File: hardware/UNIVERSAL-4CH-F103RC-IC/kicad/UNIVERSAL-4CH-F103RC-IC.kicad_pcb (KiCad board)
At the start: 2 copper layers, 124 x 93 mm, 145 parts, among them J1 ACTUATOR_CH1_4P, J2 ACTUATOR_CH2_4P, J201 REED_A_OPEN_5V_SIG_GND_PROTEC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, J202 REED_A_CLOSED_5V_SIG_GND_PROT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, J203 REED_A_IN_PLACE_5V_SIG_GND_PR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, J211 CAP_CS1_GND, J212 CAP_CS2_GND, J213 CAP_CS3_GND, J220 SWD_S1_3V3_DIO_CLK_NRST_GND, J230 LOGIC_12V_GND, J240 CANH_CANL_GND_SHIELD, J280B WIRE_FROM_C280_POS, J3 ACTUATOR_CH3_4P, J4 ACTUATOR_CH4_4P, U1 VNH5019A-E, U2 VNH5019A-E, U230 AMS1117-3V3, U250 25LC256_SOIC8_CARRIER_ID, U270 TLV6700DDCR_POWER_MONITOR, U3 VNH5019A-E, U300 STM32F103RCT6, U4 VNH5019A-E, Y300 8MHz

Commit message: Reinforce four-channel motor layer transitions
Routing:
- net CH4_OUTB: track 43.7 -> 48.5 mm, vias 1 -> 4
- net CH4_OUTA: vias 10 -> 22
- net CH3_OUTA: vias 8 -> 20
- net CH2_OUTA: vias 3 -> 5
- net CH1_OUTA: vias 3 -> 5

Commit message: Expand channel 1 and 2 power via banks
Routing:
- net CH2_OUTA: track 51.1 -> 52.7 mm, vias 5 -> 7
- net CH1_OUTA: vias 5 -> 10
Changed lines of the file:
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@@
+	)
+	(segment
+		(start 52.5 25.75)
+		(end 52.5 26.55)
+		(width 0.6)
+		(layer "F.Cu")
+		(net "CH2_OUTA")
 	)
 	(segment
@@
 	)
 	(via
+		(at 52.5 26.55)
+		(size 0.8)
+		(drill 0.4)
+		(layers "F.Cu" "B.Cu")
+		(net "CH2_OUTA")
+	)
+	(via
 		(at 53.8051 25.109)
 		(size 0.6)
 		(drill 0.3)
+		(layers "F.Cu" "B.Cu")
+		(net "CH2_OUTA")
+	)
+	(via
+		(at 52.5 25.75)
+		(size 0.8)
+		(drill 0.4)
 		(layers "F.Cu" "B.Cu")
 		(net "CH2_OUTA")
@@
 	)
 	(segment
+		(start 52.5 25.75)
+		(end 52.5 26.55)
+		(width 0.6)
+		(layer "B.Cu")
+		(net "CH2_OUTA")
+	)
+	(segment
 		(start 44.6993 17.5)
 		(end 46.6483 19.449)
@@
 	)
 	(via
+		(at 16 30.5)
+		(size 0.8)
+		(drill 0.4)
+		(layers "F.Cu" "B.Cu")
+		(net "CH1_OUTA")
+	)
+	(via
 		(at 14.9983 32.9423)
 		(size 0.6)
@@
 	)
 	(via
+		(at 14.5 30.5)
+		(size 0.8)
+		(drill 0.4)
+		(layers "F.Cu" "B.Cu")
+		(net "CH1_OUTA")
+	)
+	(via
 		(at 15.6483 32.9423)
 		(size 0.6)
@@
 	)
 	(via
+		(at 14.5 31.5)
+		(size 0.8)
+		(drill 0.4)
+		(layers "F.Cu" "B.Cu")
+		(net "CH1_OUTA")
+	)
+	(via
 		(at 7.3767 32.9423)
 		(size 0.6)
@@
 	)
 	(via
+		(at 15.25 30.5)
+		(size 0.8)
+		(drill 0.4)
+		(layers "F.Cu" "B.Cu")
+		(net "CH1_OUTA")
+	)
+	(via
 		(at 16.2983 32.9423)
 		(size 0.6)
@@
 		(layers "F.Cu" "B.Cu")
 		(net "CH1_OUTA")
+	)
+	(via
+		(at 15.25 31.5)
+		(size 0.8)
+		(drill 0.4)
+		(layers "F.Cu" "B.Cu")
+		(net "CH1_OUTA")

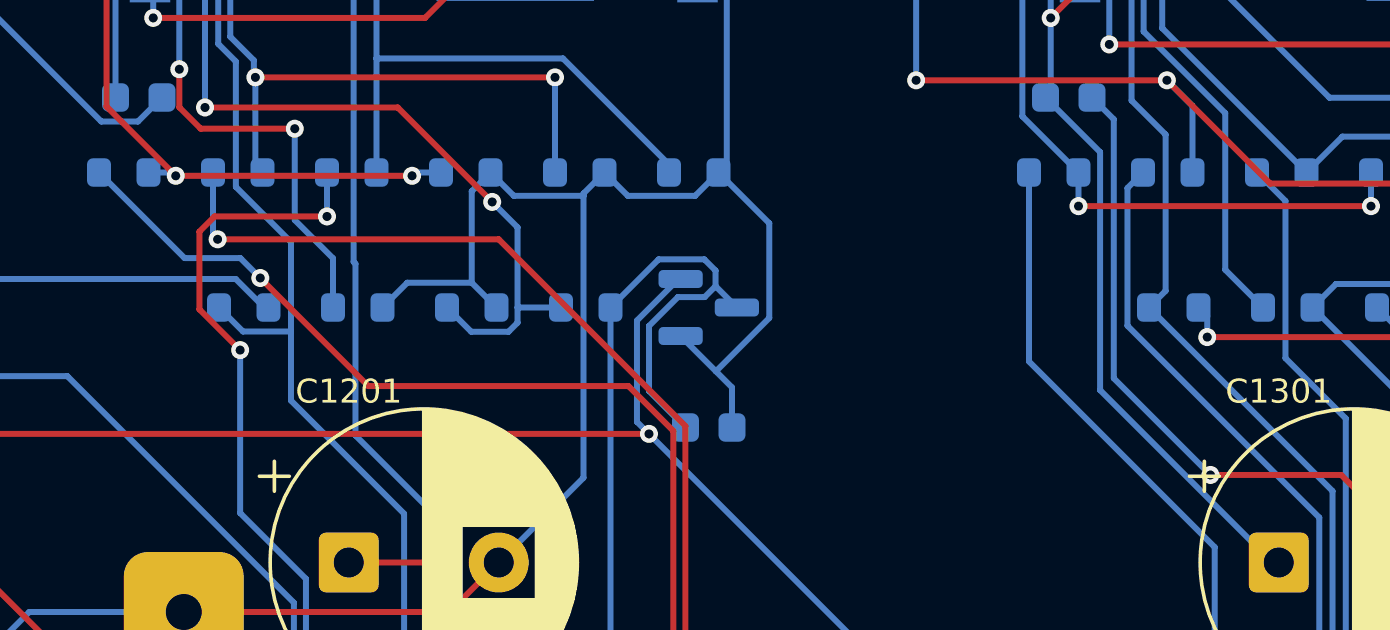
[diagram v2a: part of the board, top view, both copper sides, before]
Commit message: Add audited four-channel F103RC controller firmware
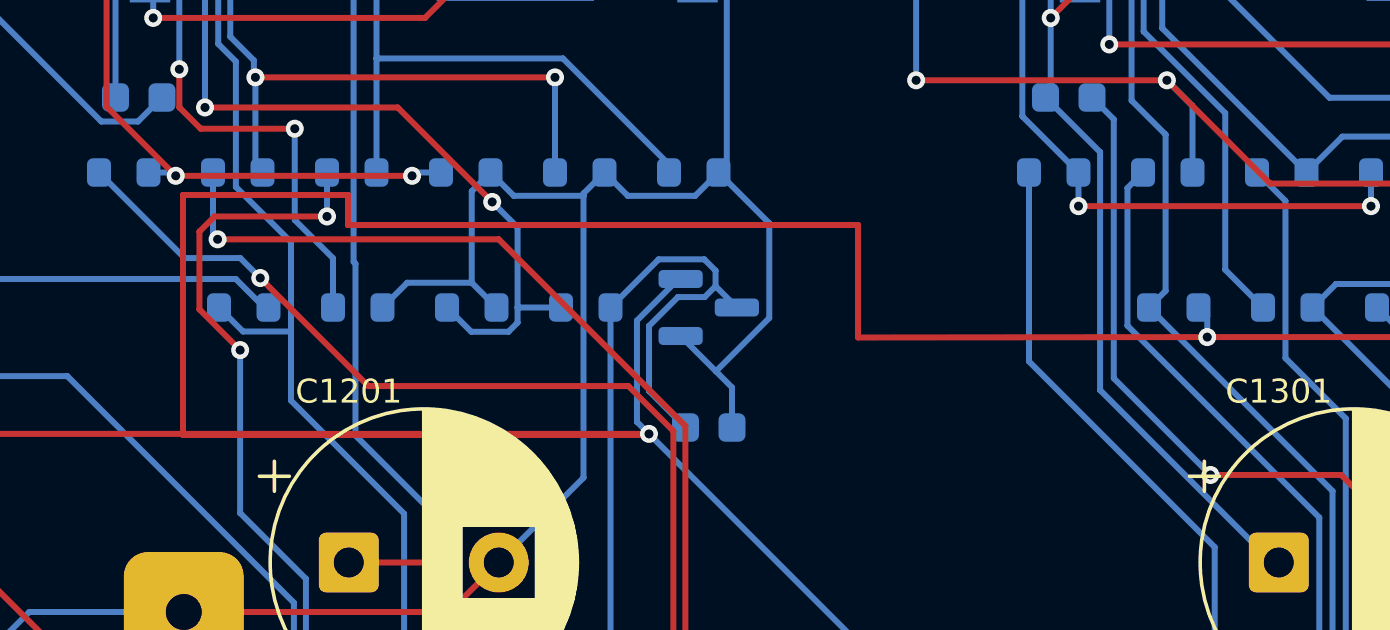
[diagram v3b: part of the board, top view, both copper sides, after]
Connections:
- D1301 pad 2: S2_3V3 -> S1_3V3
- D1401 pad 2: S2_3V3 -> S1_3V3
- R1307 pad 2: S2_3V3 -> S1_3V3
- R1407 pad 2: S2_3V3 -> S1_3V3
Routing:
- net S1_3V3: track 332.7 -> 447.1 mm, vias 6 -> 10
- net S2_3V3: track 51.9 -> 0.00 mm, vias 4 -> 0
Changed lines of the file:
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@@
 			(layers "B.Cu" "B.Mask" "B.Paste")
 			(roundrect_rratio 0.25)
-			(net "S2_3V3")
+			(net "S1_3V3")
 		)
 		(pad "3" smd roundrect
@@
 			(layers "B.Cu" "B.Mask" "B.Paste")
 			(roundrect_rratio 0.25)
-			(net "S2_3V3")
+			(net "S1_3V3")
 		)
 		(embedded_fonts no)
@@
 			(layers "B.Cu" "B.Mask" "B.Paste")
 			(roundrect_rratio 0.25)
-			(net "S2_3V3")
+			(net "S1_3V3")
 		)
 		(pad "3" smd roundrect
@@
 			(layers "B.Cu" "B.Mask" "B.Paste")
 			(roundrect_rratio 0.25)
-			(net "S2_3V3")
+			(net "S1_3V3")
 		)
 		(embedded_fonts no)
@@
 	)
 	(segment
+		(start 38.5 38.25)
+		(end 38.5 46.25)
+		(width 0.2)
+		(layer "F.Cu")
+		(net "S1_3V3")
+	)
+	(segment
 		(start 89.1847 59.381)
 		(end 89.1847 59.8418)
@@
 	)
 	(segment
+		(start 72.641 42.986)
+		(end 61 43)
+		(width 0.2)
+		(layer "F.Cu")
+		(net "S1_3V3")
+	)
+	(segment
+		(start 54 46.25)
+		(end 54.033 46.213)
+		(width 0.2)
+		(layer "F.Cu")
+		(net "S1_3V3")
+	)
+	(segment
 		(start 103.8444 59.381)
 		(end 103.7753 59.3119)
@@
 	)
 	(segment
+		(start 61 43)
+		(end 61 39.25)
+		(width 0.2)
+		(layer "F.Cu")
+		(net "S1_3V3")
+	)
+	(segment
+		(start 38.5 46.25)
+		(end 54 46.25)
+		(width 0.2)
+		(layer "F.Cu")
+		(net "S1_3V3")
+	)
+	(segment
 		(start 10.5465 43.4709)
 		(end 25.2327 43.4709)
@@
 	)
 	(segment
+		(start 103.3484 39.6332)
+		(end 103.4701 39.7549)
+		(width 0.2)
+		(layer "F.Cu")
+		(net "S1_3V3")
+	)
+	(segment
+		(start 103.3484 39.6332)
+		(end 86.2212 39.6332)
+		(width 0.2)
+		(layer "F.Cu")
+		(net "S1_3V3")
+	)
+	(segment
 		(start 103.7753 59.3119)
 		(end 89.2538 59.3119)
@@
 	)
 	(segment
+		(start 86.0875 39.7669)
+		(end 82.868 42.9864)
+		(width 0.2)
+		(layer "F.Cu")
+		(net "S1_3V3")
+	)
+	(segment
+		(start 103.4701 39.7549)
+		(end 117.0875 39.7549)
+		(width 0.2)
+		(layer "F.Cu")
+		(net "S1_3V3")
+	)
+	(segment
+		(start 61 39.25)
+		(end 44 39.25)
+		(width 0.2)
+		(layer "F.Cu")
+		(net "S1_3V3")
+	)
+	(segment
 		(start 69.9071 60.5)
 		(end 68.275 62.1321)
@@
 	)
 	(segment
+		(start 44 39.25)
+		(end 44 38.25)
+		(width 0.2)
+		(layer "F.Cu")
+		(net "S1_3V3")
+	)
+	(segment
 		(start 25.2327 43.4709)
 		(end 27.9749 46.2131)
@@
 		(net "S1_3V3")
 	)
+	(segment
+		(start 44 38.25)
+		(end 38.5 38.25)
+		(width 0.2)
+		(layer "F.Cu")
+		(net "S1_3V3")
+	)
+	(segment
+		(start 82.868 42.9864)
+		(end 72.6413 42.9864)
+		(width 0.2)
+		(layer "F.Cu")
+		(net "S1_3V3")
+	)
+	(segment
+		(start 86.2212 39.6332)
+		(end 86.0875 39.7669)
+		(width 0.2)
+		(layer "F.Cu")
+		(net "S1_3V3")
+	)
+	(via
+		(at 103.3484 39.6332)
+		(size 0.6)
+		(drill 0.3)
+		(layers "F.Cu" "B.Cu")
+		(net "S1_3V3")
+	)
+	(via
+		(at 86.0875 39.7669)
+		(size 0.6)
+		(drill 0.3)
+		(layers "F.Cu" "B.Cu")
+		(net "S1_3V3")
+	)
 	(via
 		(at 10.5465 43.4709)
@@
 	)
 	(via
+		(at 72.6413 42.9864)
+		(size 0.6)
+		(drill 0.3)
+		(layers "F.Cu" "B.Cu")
+		(net "S1_3V3")
+	)
+	(via
 		(at 87.292 61.4943)
 		(size 0.6)
@@
 	)
 	(via
+		(at 117.0875 39.7549)
+		(size 0.6)
+		(drill 0.3)
+		(layers "F.Cu" "B.Cu")
+		(net "S1_3V3")
+	)
+	(via
 		(at 25.2327 43.4709)
 		(size 0.6)
@@
 	)
 	(segment
+		(start 86.0875 41.05)
+		(end 86.0875 39.7669)
+		(width 0.2)
+		(layer "B.Cu")
+		(net "S1_3V3")
+	)
+	(segment
 		(start 60.7765 70.3744)
 		(end 62.5791 68.5718)
@@
 	)
 	(segment
+		(start 117.0875 41.05)
+		(end 117.0875 39.7549)
+		(width 0.2)
+		(layer "B.Cu")
+		(net "S1_3V3")
+	)
+	(segment
 		(start 46.6192 69.413)
 		(end 48.3414 67.6908)
@@
 	)
 	(segment
+		(start 103.35 42)
+		(end 103.35 39.6348)
+		(width 0.2)
+		(layer "B.Cu")
+		(net "S1_3V3")
+	)
+	(segment
 		(start 80.2284 76.3249)
 		(end 79.8267 75.9232)
@@
 	)
 	(segment
+		(start 72.35 42)
+		(end 72.6413 42.2913)
+		(width 0.2)
+		(layer "B.Cu")
+		(net "S1_3V3")
+	)
+	(segment
 		(start 69.27 60.825)
 		(end 68.275 60.825)
@@
 	)
 	(segment
+		(start 72.6413 42.2913)
+		(end 72.6413 42.9864)
+		(width 0.2)
+		(layer "B.Cu")
+		(net "S1_3V3")
+	)
+	(segment
 		(start 58.5609 56.6891)
 		(end 57.75 57.5)
@@
 	)
 	(segment
+		(start 103.35 39.6348)
+		(end 103.3484 39.6332)
+		(width 0.2)
+		(layer "B.Cu")
+		(net "S1_3V3")
+	)
+	(segment
 		(start 66.5466 56.7034)
 		(end 65.75 57.5)
@@
 	)
 	(segment
-		(start 103.3484 39.6332)
-		(end 103.4701 39.7549)
-		(width 0.2)
-		(layer "F.Cu")
-		(net "S2_3V3")
-	)
-	(segment
-		(start 103.3484 39.6332)
-		(end 86.2212 39.6332)
-		(width 0.2)
-		(layer "F.Cu")
-		(net "S2_3V3")
-	)
-	(segment
-		(start 86.0875 39.7669)
-		(end 82.868 42.9864)
-		(width 0.2)
-		(layer "F.Cu")
-		(net "S2_3V3")
-	)
-	(segment
-		(start 103.4701 39.7549)
-		(end 117.0875 39.7549)
-		(width 0.2)
-		(layer "F.Cu")
-		(net "S2_3V3")
-	)
-	(segment
-		(start 82.868 42.9864)
-		(end 72.6413 42.9864)
-		(width 0.2)
-		(layer "F.Cu")
-		(net "S2_3V3")
-	)
-	(segment
-		(start 86.2212 39.6332)
-		(end 86.0875 39.7669)
-		(width 0.2)
-		(layer "F.Cu")
-		(net "S2_3V3")
-	)
-	(via
-		(at 103.3484 39.6332)
-		(size 0.6)
-		(drill 0.3)
-		(layers "F.Cu" "B.Cu")
-		(net "S2_3V3")
-	)
-	(via
-		(at 86.0875 39.7669)
-		(size 0.6)
-		(drill 0.3)
-		(layers "F.Cu" "B.Cu")
-		(net "S2_3V3")
-	)
-	(via
-		(at 72.6413 42.9864)
-		(size 0.6)
-		(drill 0.3)
-		(layers "F.Cu" "B.Cu")
-		(net "S2_3V3")
-	)
-	(via
-		(at 117.0875 39.7549)
-		(size 0.6)
-		(drill 0.3)
-		(layers "F.Cu" "B.Cu")
-		(net "S2_3V3")
-	)
-	(segment
-		(start 86.0875 41.05)
-		(end 86.0875 39.7669)
-		(width 0.2)
-		(layer "B.Cu")
-		(net "S2_3V3")
-	)
-	(segment
-		(start 117.0875 41.05)
-		(end 117.0875 39.7549)
-		(width 0.2)
-		(layer "B.Cu")
-		(net "S2_3V3")
-	)
-	(segment
-		(start 103.35 42)
-		(end 103.35 39.6348)
-		(width 0.2)
-		(layer "B.Cu")
-		(net "S2_3V3")
-	)
-	(segment
-		(start 72.35 42)
-		(end 72.6413 42.2913)
-		(width 0.2)
-		(layer "B.Cu")
-		(net "S2_3V3")
-	)
-	(segment
-		(start 72.6413 42.2913)
-		(end 72.6413 42.9864)
-		(width 0.2)
-		(layer "B.Cu")
-		(net "S2_3V3")
-	)
-	(segment
-		(start 103.35 39.6348)
-		(end 103.3484 39.6332)
-		(width 0.2)
-		(layer "B.Cu")
-		(net "S2_3V3")
-	)
-	(segment
